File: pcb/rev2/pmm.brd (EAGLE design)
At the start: 78.6 x 43 mm, 45 parts, among them IC3 STM32F042F4, J1 AUDIO_JACK_3.5MM_PTH, J2 FFC3B07-05-T, SW4 324_SW, U2 USBC_16P, U4 XC6206_DEV

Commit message: working on improvments
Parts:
- added TP1, TP2, TP3: TPTP18R, testpad:TP18R
- moved R8 34.1 mm to (14.4, -9.53), flipped to the bottom
- moved U$1 33.4 mm to (25.0, -23.0)
- moved C3 21.9 mm to (27.3, -12.7), flipped to the bottom, turned to 180 degrees
- moved R9 0.36 mm to (17.0, -17.8), turned to 180 degrees
- moved JP3 0.26 mm to (17.9, -20.4)
- moved J2 0.13 mm to (-19.0, -21.1), flipped to the top
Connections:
- net +3V3: now also TP3.TP
- net GND: now also TP2.TP
- net LS_EXT: now also JP3.1
- net LS_INTERNAL: now also JP3.3
- net LS_MCU: now also TP1.TP
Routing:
- net LS_INTERNAL: track 0.00 -> 61.1 mm
- net LS_EXT: track 0.00 -> 41.3 mm
- net +3V3: track 106.1 -> 143.9 mm, vias 4 -> 6
- net LS_MCU: track 0.00 -> 15.3 mm
- net N$3: track 25.7 -> 29.7 mm, vias 1 -> 0
- net BUTTON2: track 41.0 -> 37.0 mm
- net GND: vias 6 -> 9
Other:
- board text added: "3"
- board text added: "EXT"
- board text added: "INT"
- board text added: "LS"
- board text added: "PulseHPT.com dekuNukem 2024"
- board text removed: "PulseHPT.com dekuNukem 2023"

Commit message: working on improvments
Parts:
- moved U$17 0.13 mm to (-30.4, -14.5)
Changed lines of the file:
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@@
 <setting verticaltext="up"/>
 </settings>
-<grid distance="5" unitdist="mil" unit="mil" style="lines" multiple="1" display="no" altdistance="1" altunitdist="mil" altunit="mil"/>
+<grid distance="10" unitdist="mil" unit="mil" style="lines" multiple="1" display="no" altdistance="1" altunitdist="mil" altunit="mil"/>
 <layers>
 <layer number="1" name="Top" color="4" fill="1" visible="yes" active="yes"/>
@@
 <layer number="14" name="Route14" color="22" fill="1" visible="no" active="no"/>
 <layer number="15" name="Route15" color="23" fill="1" visible="no" active="no"/>
-<layer number="16" name="Bottom" color="1" fill="1" visible="no" active="yes"/>
+<layer number="16" name="Bottom" color="1" fill="1" visible="yes" active="yes"/>
 <layer number="17" name="Pads" color="2" fill="1" visible="yes" active="yes"/>
 <layer number="18" name="Vias" color="2" fill="1" visible="yes" active="yes"/>
 <layer number="19" name="Unrouted" color="6" fill="1" visible="yes" active="yes"/>
 <layer number="20" name="Dimension" color="24" fill="1" visible="yes" active="yes"/>
-<layer number="21" name="tPlace" color="7" fill="1" visible="no" active="yes"/>
-<layer number="22" name="bPlace" color="7" fill="1" visible="no" active="yes"/>
+<layer number="21" name="tPlace" color="7" fill="1" visible="yes" active="yes"/>
+<layer number="22" name="bPlace" color="7" fill="1" visible="yes" active="yes"/>
 <layer number="23" name="tOrigins" color="15" fill="1" visible="yes" active="yes"/>
-<layer number="24" name="bOrigins" color="15" fill="1" visible="no" active="yes"/>
-<layer number="25" name="tNames" color="7" fill="1" visible="no" active="yes"/>
-<layer number="26" name="bNames" color="7" fill="1" visible="no" active="yes"/>
-<layer number="27" name="tValues" color="7" fill="1" visible="no" active="yes"/>
-<layer number="28" name="bValues" color="7" fill="1" visible="no" active="yes"/>
+<layer number="24" name="bOrigins" color="15" fill="1" visible="yes" active="yes"/>
+<layer number="25" name="tNames" color="7" fill="1" visible="yes" active="yes"/>
+<layer number="26" name="bNames" color="7" fill="1" visible="yes" active="yes"/>
+<layer number="27" name="tValues" color="7" fill="1" visible="yes" active="yes"/>
+<layer number="28" name="bValues" color="7" fill="1" visible="yes" active="yes"/>
 <layer number="29" name="tStop" color="7" fill="3" visible="no" active="yes"/>
 <layer number="30" name="bStop" color="7" fill="6" visible="no" active="yes"/>
@@
 <layer number="38" name="bTest" color="7" fill="1" visible="no" active="yes"/>
 <layer number="39" name="tKeepout" color="4" fill="11" visible="yes" active="yes"/>
-<layer number="40" name="bKeepout" color="1" fill="11" visible="no" active="yes"/>
+<layer number="40" name="bKeepout" color="1" fill="11" visible="yes" active="yes"/>
 <layer number="41" name="tRestrict" color="4" fill="10" visible="yes" active="yes"/>
-<layer number="42" name="bRestrict" color="1" fill="10" visible="no" active="yes"/>
+<layer number="42" name="bRestrict" color="1" fill="10" visible="yes" active="yes"/>
 <layer number="43" name="vRestrict" color="2" fill="10" visible="no" active="yes"/>
 <layer number="44" name="Drills" color="7" fill="1" visible="no" active="yes"/>
@@
 <layer number="49" name="Reference" color="7" fill="1" visible="no" active="yes"/>
 <layer number="50" name="dxf" color="7" fill="1" visible="no" active="no"/>
-<layer number="51" name="tDocu" color="7" fill="1" visible="no" active="yes"/>
-<layer number="52" name="bDocu" color="7" fill="1" visible="no" active="yes"/>
+<layer number="51" name="tDocu" color="7" fill="1" visible="yes" active="yes"/>
+<layer number="52" name="bDocu" color="7" fill="1" visible="yes" active="yes"/>
 <layer number="53" name="tGND_GNDA" color="7" fill="1" visible="no" active="no"/>
 <layer number="54" name="bGND_GNDA" color="7" fill="1" visible="no" active="no"/>
@@
 <element name="U$11" library="apricot" package="HOTSHOE_RAIL_NOPASTE" value="HOTSHOE_NOPASTE" x="-1.397" y="9.398" smashed="yes" rot="MR0"/>
 <element name="U$13" library="apricot" package="HOTSHOE_RAIL_NOPASTE" value="HOTSHOE_NOPASTE" x="14.097" y="9.398" smashed="yes" rot="MR0"/>
-<element name="U$17" library="apricot" package="LS" value="LS_HOLE" x="-30.226" y="-14.478" smashed="yes"/>
+<element name="U$17" library="apricot" package="LS" value="LS_HOLE" x="-30.353" y="-14.478" smashed="yes"/>
 <element name="JP3" library="adafruit_changed" package="1X03-CLEANBIG" value="" x="17.907" y="-20.373" smashed="yes">
 <attribute name="VALUE" x="14.097" y="-23.548" size="1.27" layer="27"/>
@@
 <wire x1="-25.654" y1="-18.923" x2="-25.654" y2="-12.113" width="0.3048" layer="16"/>
 <wire x1="-25.654" y1="-12.113" x2="-27.099" y2="-10.668" width="0.3048" layer="16"/>
-<wire x1="-27.099" y1="-10.668" x2="-28.0162" y2="-9.7508" width="0.3048" layer="16"/>
-<wire x1="-28.0162" y1="-9.7508" x2="-28.0162" y2="-8.382" width="0.3048" layer="16"/>
-<wire x1="-28.0162" y1="-8.382" x2="-28.0162" y2="-9.7508" width="0.3048" layer="1"/>
-<wire x1="-28.0162" y1="-9.7508" x2="-27.099" y2="-10.668" width="0.3048" layer="1"/>
+<wire x1="-27.099" y1="-10.668" x2="-28.1432" y2="-9.6238" width="0.3048" layer="16"/>
+<wire x1="-28.1432" y1="-9.6238" x2="-28.1432" y2="-8.382" width="0.3048" layer="16"/>
+<wire x1="-28.1432" y1="-8.382" x2="-28.1432" y2="-9.6238" width="0.3048" layer="1"/>
+<wire x1="-28.1432" y1="-9.6238" x2="-27.099" y2="-10.668" width="0.3048" layer="1"/>
 <via x="-20.193" y="-21.082" extent="1-16" drill="0.5"/>
 <wire x1="-19.971" y1="-18.632" x2="-19.971" y2="-20.86" width="0.3048" layer="1"/>
@@
 <wire x1="-21.384" y1="-9.025" x2="-25.826" y2="-9.025" width="0.3048" layer="1"/>
 <wire x1="-25.826" y1="-9.025" x2="-25.956" y2="-9.155" width="0.3048" layer="1"/>
-<wire x1="-28.0162" y1="-8.382" x2="-27.2432" y2="-9.155" width="0.3048" layer="1"/>
-<wire x1="-27.2432" y1="-9.155" x2="-25.956" y2="-9.155" width="0.3048" layer="1"/>
+<wire x1="-28.1432" y1="-8.382" x2="-27.3702" y2="-9.155" width="0.3048" layer="1"/>
+<wire x1="-27.3702" y1="-9.155" x2="-25.956" y2="-9.155" width="0.3048" layer="1"/>
 <wire x1="12.827" y1="-3.81" x2="6.3" y2="-10.337" width="0.4064" layer="16"/>
 <wire x1="6.3" y1="-10.337" x2="6.3" y2="-20.373" width="0.4064" layer="16"/>
@@
 <contactref element="U4" pad="2"/>
 <contactref element="JP1" pad="3"/>
-<wire x1="33.036" y1="-23.81" x2="29.779" y2="-23.81" width="0.3048" layer="1"/>
-<wire x1="29.779" y1="-23.81" x2="24.892" y2="-18.923" width="0.3048" layer="1"/>
-<wire x1="24.892" y1="-18.923" x2="19.558" y2="-18.923" width="0.3048" layer="1"/>
-<wire x1="19.558" y1="-18.923" x2="19.177" y2="-19.304" width="0.3048" layer="1"/>
+<wire x1="33.036" y1="-23.81" x2="30.541" y2="-23.81" width="0.3048" layer="1"/>
+<wire x1="30.541" y1="-23.81" x2="25.4" y2="-18.669" width="0.3048" layer="1"/>
+<wire x1="25.4" y1="-18.669" x2="19.812" y2="-18.669" width="0.3048" layer="1"/>
+<wire x1="19.812" y1="-18.669" x2="19.177" y2="-19.304" width="0.3048" layer="1"/>
 <wire x1="19.177" y1="-19.304" x2="19.177" y2="-21.463" width="0.3048" layer="1"/>
 <wire x1="19.177" y1="-21.463" x2="18.288" y2="-22.352" width="0.3048" layer="1"/>
@@
 <contactref element="U$17" pad="B3"/>
 <contactref element="JP3" pad="3"/>
-<wire x1="-28.0162" y1="-20.701" x2="-24.7142" y2="-24.003" width="0.2032" layer="1"/>
-<wire x1="-24.7142" y1="-24.003" x2="-1.651" y2="-24.003" width="0.2032" layer="1"/>
+<wire x1="-28.1432" y1="-20.701" x2="-24.8412" y2="-24.003" width="0.2032" layer="1"/>
+<wire x1="-24.8412" y1="-24.003" x2="-1.651" y2="-24.003" width="0.2032" layer="1"/>
 <wire x1="-1.651" y1="-24.003" x2="0.635" y2="-21.717" width="0.2032" layer="1"/>
 <wire x1="0.635" y1="-21.717" x2="10.922" y2="-21.717" width="0.2032" layer="1"/>
@@
 <wire x1="20.447" y1="-21.844" x2="20.447" y2="-20.373" width="0.2032" layer="1"/>
 <wire x1="19.05" y1="-23.241" x2="20.447" y2="-21.844" width="0.2032" layer="1"/>
-<wire x1="-30.734" y1="-20.701" x2="-30.734" y2="-18.288" width="0.3048" layer="1"/>
-<wire x1="-30.734" y1="-18.288" x2="-30.607" y2="-18.161" width="0.3048" layer="1"/>
-<wire x1="-30.607" y1="-18.161" x2="-28.194" y2="-18.161" width="0.3048" layer="1"/>
-<wire x1="-28.0162" y1="-18.3388" x2="-28.0162" y2="-20.701" width="0.3048" layer="1"/>
-<wire x1="-28.194" y1="-18.161" x2="-28.0162" y2="-18.3388" width="0.3048" layer="1"/>
-<wire x1="-30.734" y1="-20.701" x2="-30.734" y2="-20.701" width="0" layer="19" extent="1-16"/>
-<wire x1="-28.0162" y1="-20.701" x2="-28.0162" y2="-20.701" width="0" layer="19" extent="1-16"/>
+<wire x1="-30.861" y1="-20.701" x2="-30.861" y2="-18.288" width="0.3048" layer="1"/>
+<wire x1="-30.861" y1="-18.288" x2="-30.734" y2="-18.161" width="0.3048" layer="1"/>
+<wire x1="-30.734" y1="-18.161" x2="-28.321" y2="-18.161" width="0.3048" layer="1"/>
+<wire x1="-28.1432" y1="-18.3388" x2="-28.1432" y2="-20.701" width="0.3048" layer="1"/>
+<wire x1="-28.321" y1="-18.161" x2="-28.1432" y2="-18.3388" width="0.3048" layer="1"/>
+<wire x1="-30.861" y1="-20.701" x2="-30.861" y2="-20.701" width="0" layer="19" extent="1-16"/>
+<wire x1="-28.1432" y1="-20.701" x2="-28.1432" y2="-20.701" width="0" layer="19" extent="1-16"/>
 </signal>
 <signal name="LS_EXT">

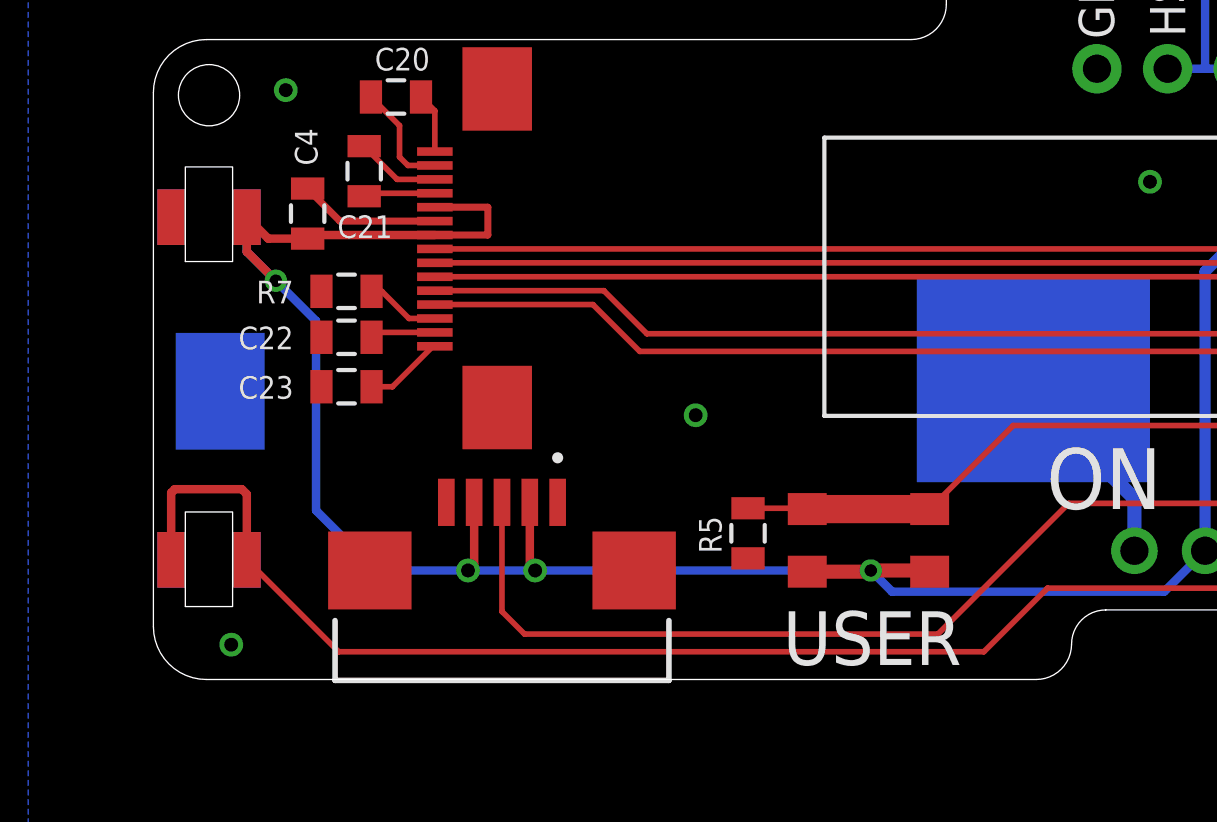
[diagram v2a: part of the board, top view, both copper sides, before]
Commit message: adjusted for pcb thickness
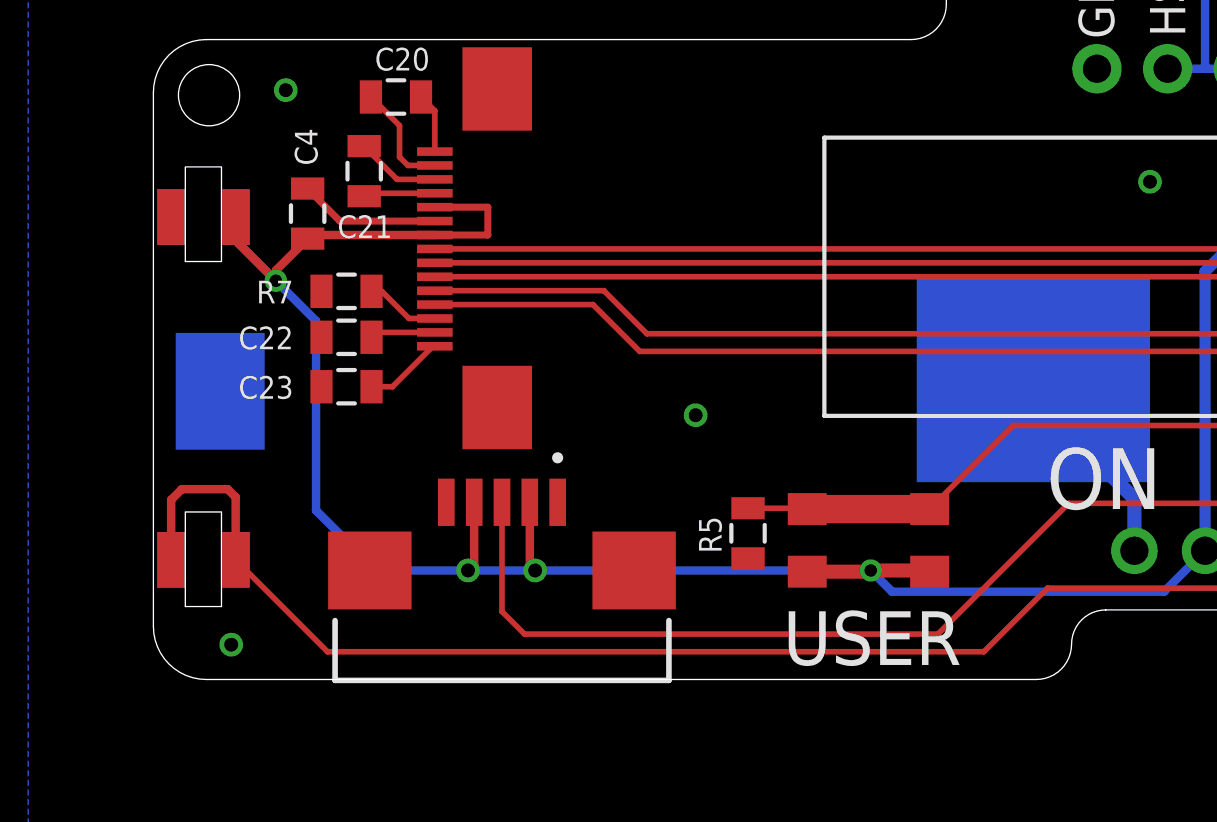
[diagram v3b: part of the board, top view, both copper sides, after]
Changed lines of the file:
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@@
 <wire x1="-25.654" y1="-18.923" x2="-25.654" y2="-12.113" width="0.3048" layer="16"/>
 <wire x1="-25.654" y1="-12.113" x2="-27.099" y2="-10.668" width="0.3048" layer="16"/>
-<wire x1="-27.099" y1="-10.668" x2="-28.1432" y2="-9.6238" width="0.3048" layer="16"/>
-<wire x1="-28.1432" y1="-9.6238" x2="-28.1432" y2="-8.382" width="0.3048" layer="16"/>
-<wire x1="-28.1432" y1="-8.382" x2="-28.1432" y2="-9.6238" width="0.3048" layer="1"/>
-<wire x1="-28.1432" y1="-9.6238" x2="-27.099" y2="-10.668" width="0.3048" layer="1"/>
 <via x="-20.193" y="-21.082" extent="1-16" drill="0.5"/>
 <wire x1="-19.971" y1="-18.632" x2="-19.971" y2="-20.86" width="0.3048" layer="1"/>
@@
 <wire x1="-21.384" y1="-9.025" x2="-25.826" y2="-9.025" width="0.3048" layer="1"/>
 <wire x1="-25.826" y1="-9.025" x2="-25.956" y2="-9.155" width="0.3048" layer="1"/>
-<wire x1="-28.1432" y1="-8.382" x2="-27.3702" y2="-9.155" width="0.3048" layer="1"/>
-<wire x1="-27.3702" y1="-9.155" x2="-25.956" y2="-9.155" width="0.3048" layer="1"/>
 <wire x1="12.827" y1="-3.81" x2="6.3" y2="-10.337" width="0.4064" layer="16"/>
 <wire x1="6.3" y1="-10.337" x2="6.3" y2="-20.373" width="0.4064" layer="16"/>
@@
 <wire x1="13.589" y1="-21.844" x2="15.367" y2="-23.622" width="0.3048" layer="16"/>
 <wire x1="7.771" y1="-21.844" x2="13.589" y2="-21.844" width="0.3048" layer="16"/>
+<wire x1="-28.5432" y1="-9.2238" x2="-28.5432" y2="-8.382" width="0.3048" layer="1"/>
+<wire x1="-27.099" y1="-10.668" x2="-28.5432" y2="-9.2238" width="0.3048" layer="1"/>
+<wire x1="-27.099" y1="-10.668" x2="-27.099" y2="-10.298" width="0.3048" layer="1"/>
+<wire x1="-27.099" y1="-10.298" x2="-25.956" y2="-9.155" width="0.3048" layer="1"/>
+<wire x1="-28.5432" y1="-8.382" x2="-28.5432" y2="-9.2238" width="0.3048" layer="16"/>
+<wire x1="-28.5432" y1="-9.2238" x2="-27.099" y2="-10.668" width="0.3048" layer="16"/>
 </signal>
 <signal name="USB_DP">
@@
 <contactref element="U$17" pad="B3"/>
 <contactref element="JP3" pad="3"/>
-<wire x1="-28.1432" y1="-20.701" x2="-24.8412" y2="-24.003" width="0.2032" layer="1"/>
-<wire x1="-24.8412" y1="-24.003" x2="-1.651" y2="-24.003" width="0.2032" layer="1"/>
-<wire x1="-1.651" y1="-24.003" x2="0.635" y2="-21.717" width="0.2032" layer="1"/>
+<wire x1="0.635" y1="-21.717" x2="-1.651" y2="-24.003" width="0.2032" layer="1"/>
 <wire x1="0.635" y1="-21.717" x2="10.922" y2="-21.717" width="0.2032" layer="1"/>
 <wire x1="10.922" y1="-21.717" x2="12.446" y2="-23.241" width="0.2032" layer="1"/>
@@
 <wire x1="20.447" y1="-21.844" x2="20.447" y2="-20.373" width="0.2032" layer="1"/>
 <wire x1="19.05" y1="-23.241" x2="20.447" y2="-21.844" width="0.2032" layer="1"/>
-<wire x1="-30.861" y1="-20.701" x2="-30.861" y2="-18.288" width="0.3048" layer="1"/>
-<wire x1="-30.861" y1="-18.288" x2="-30.734" y2="-18.161" width="0.3048" layer="1"/>
-<wire x1="-30.734" y1="-18.161" x2="-28.321" y2="-18.161" width="0.3048" layer="1"/>
-<wire x1="-28.1432" y1="-18.3388" x2="-28.1432" y2="-20.701" width="0.3048" layer="1"/>
-<wire x1="-28.321" y1="-18.161" x2="-28.1432" y2="-18.3388" width="0.3048" layer="1"/>
+<wire x1="-30.861" y1="-20.701" x2="-30.861" y2="-18.542" width="0.3048" layer="1"/>
+<wire x1="-30.861" y1="-18.542" x2="-30.48" y2="-18.161" width="0.3048" layer="1"/>
+<wire x1="-30.48" y1="-18.161" x2="-28.829" y2="-18.161" width="0.3048" layer="1"/>
+<wire x1="-28.5432" y1="-18.4468" x2="-28.5432" y2="-20.701" width="0.3048" layer="1"/>
+<wire x1="-28.829" y1="-18.161" x2="-28.5432" y2="-18.4468" width="0.3048" layer="1"/>
+<wire x1="-25.2412" y1="-24.003" x2="-28.5432" y2="-20.701" width="0.2032" layer="1"/>
+<wire x1="-1.651" y1="-24.003" x2="-25.2412" y2="-24.003" width="0.2032" layer="1"/>
 <wire x1="-30.861" y1="-20.701" x2="-30.861" y2="-20.701" width="0" layer="19" extent="1-16"/>
-<wire x1="-28.1432" y1="-20.701" x2="-28.1432" y2="-20.701" width="0" layer="19" extent="1-16"/>
+<wire x1="-28.5432" y1="-20.701" x2="-28.5432" y2="-20.701" width="0" layer="19" extent="1-16"/>
 </signal>
 <signal name="LS_EXT">
